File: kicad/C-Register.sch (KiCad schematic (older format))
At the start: 19 parts, among them U122 74LS245, U123 74LS173, U124 74LS173

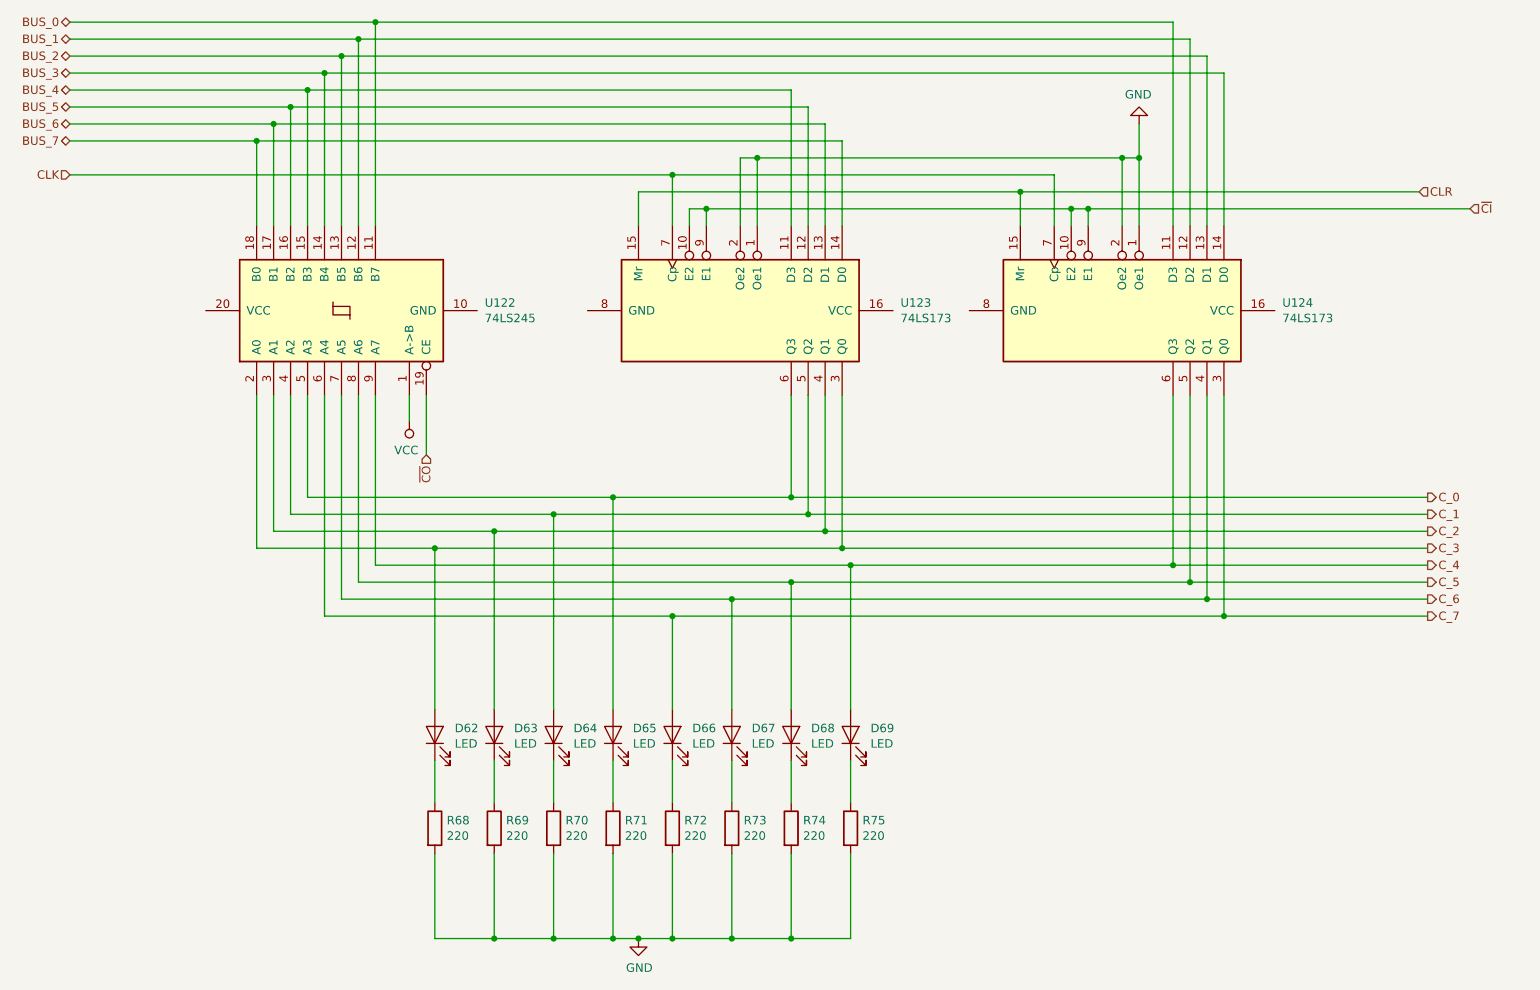
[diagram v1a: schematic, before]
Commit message: Reorganize part references
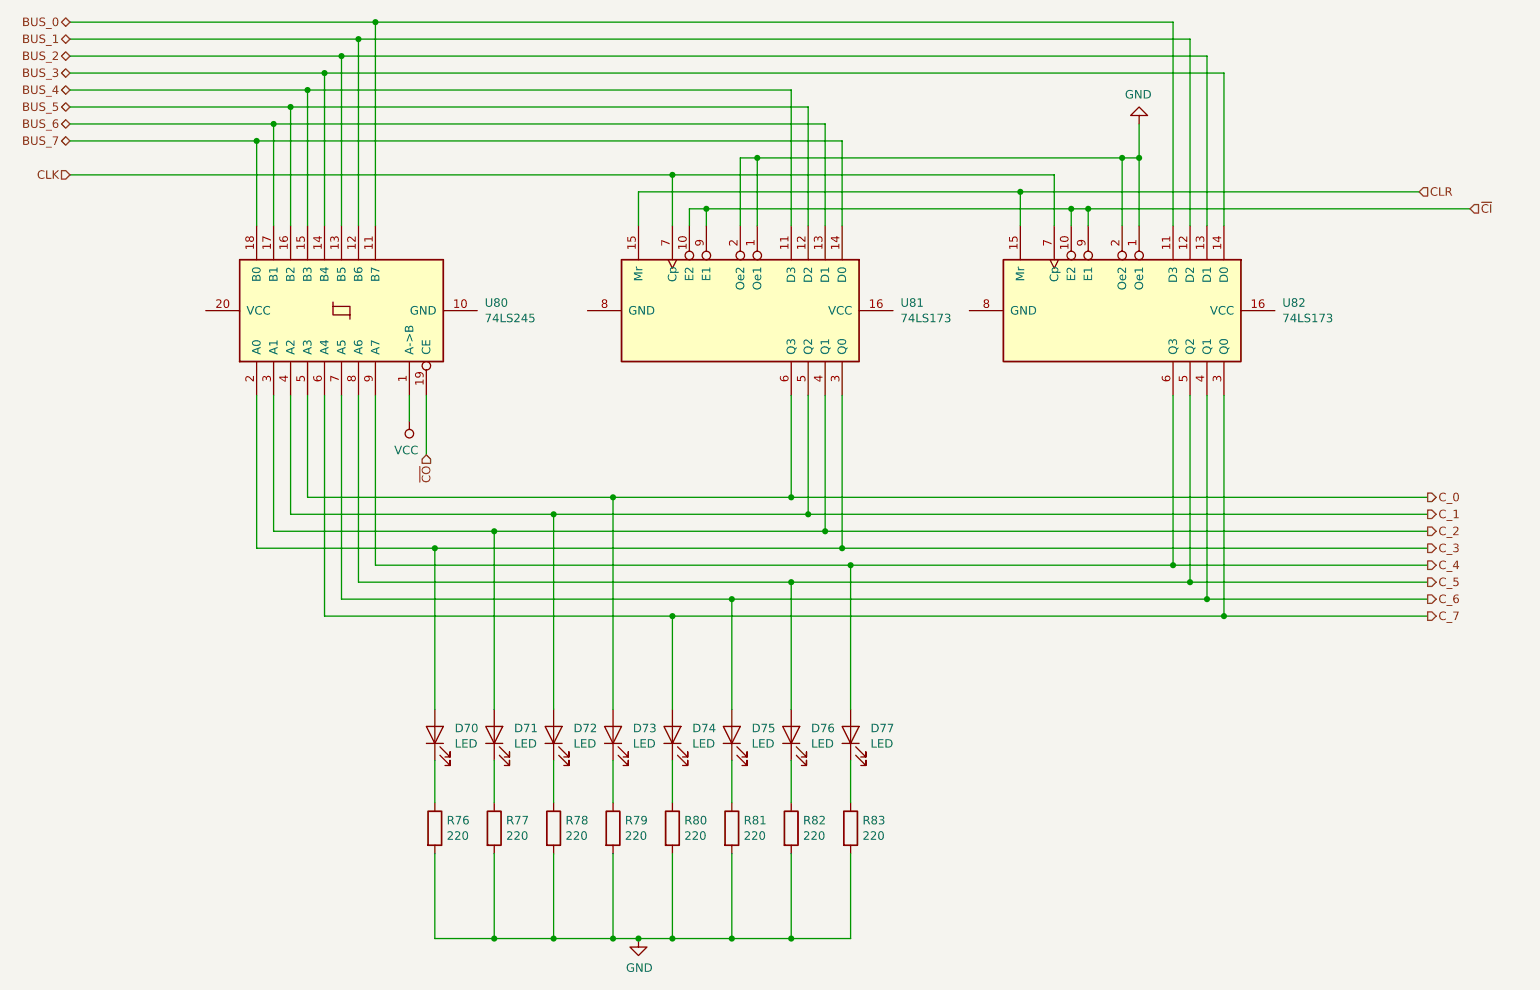
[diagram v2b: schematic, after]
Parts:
- renumbered D62 to D70, D63 to D71, D64 to D72, D65 to D73, D66 to D74, D67 to D75, D68 to D76, D69 to D77, R68 to R76, R69 to R77, R70 to R78, R71 to R79, R72 to R80, R73 to R81, R74 to R82, R75 to R83, U122 to U80, U123 to U81, U124 to U82
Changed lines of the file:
@@
 $Descr USLetter 11000 8500
 encoding utf-8
-Sheet 6 26
+Sheet 22 26
 Title "C Register"
 Date "2019-10-03"
@@
 AR Path="/5D9C722C/5D9DFD2F" Ref="U?"  Part="1"
 AR Path="/5D9DCC2F/5D9DFD2F" Ref="U?"  Part="1"
-AR Path="/5DA98D6D/5DA9A59D/5D9DFD2F" Ref="U122"  Part="1"
-F 0 "U122" V 3396 1956 50  0000 R CNN
+AR Path="/5DA98D6D/5DA9A59D/5D9DFD2F" Ref="U80"  Part="1"
+F 0 "U80" V 3396 1956 50  0000 R CNN
 F 1 "74LS245" V 3305 1956 50  0000 R CNN
 F 2 "" H 3350 2800 50  0001 C CNN
@@
 AR Path="/5D9C722C/5D9DFD5C" Ref="U?"  Part="1"
 AR Path="/5D9DCC2F/5D9DFD5C" Ref="U?"  Part="1"
-AR Path="/5DA98D6D/5DA9A59D/5D9DFD5C" Ref="U124"  Part="1"
-F 0 "U124" V 7904 3744 50  0000 L CNN
+AR Path="/5DA98D6D/5DA9A59D/5D9DFD5C" Ref="U82"  Part="1"
+F 0 "U82" V 7904 3744 50  0000 L CNN
 F 1 "74LS173" V 7995 3744 50  0000 L CNN
 F 2 "" H 7950 2800 50  0001 C CNN
@@
 AR Path="/5D9C722C/5D9DFD86" Ref="D?"  Part="1"
 AR Path="/5D9DCC2F/5D9DFD86" Ref="D?"  Part="1"
-AR Path="/5DA98D6D/5DA9A59D/5D9DFD86" Ref="D62"  Part="1"
-F 0 "D62" V 3939 5183 50  0000 R CNN
+AR Path="/5DA98D6D/5DA9A59D/5D9DFD86" Ref="D70"  Part="1"
+F 0 "D70" V 3939 5183 50  0000 R CNN
 F 1 "LED" V 3848 5183 50  0000 R CNN
 F 2 "" H 3900 5300 50  0001 C CNN
@@
 AR Path="/5D9C722C/5D9DFD8C" Ref="D?"  Part="1"
 AR Path="/5D9DCC2F/5D9DFD8C" Ref="D?"  Part="1"
-AR Path="/5DA98D6D/5DA9A59D/5D9DFD8C" Ref="D63"  Part="1"
-F 0 "D63" V 4289 5183 50  0000 R CNN
+AR Path="/5DA98D6D/5DA9A59D/5D9DFD8C" Ref="D71"  Part="1"
+F 0 "D71" V 4289 5183 50  0000 R CNN
 F 1 "LED" V 4198 5183 50  0000 R CNN
 F 2 "" H 4250 5300 50  0001 C CNN
@@
 AR Path="/5D9C722C/5D9DFD92" Ref="D?"  Part="1"
 AR Path="/5D9DCC2F/5D9DFD92" Ref="D?"  Part="1"
-AR Path="/5DA98D6D/5DA9A59D/5D9DFD92" Ref="D64"  Part="1"
-F 0 "D64" V 4639 5183 50  0000 R CNN
+AR Path="/5DA98D6D/5DA9A59D/5D9DFD92" Ref="D72"  Part="1"
+F 0 "D72" V 4639 5183 50  0000 R CNN
 F 1 "LED" V 4548 5183 50  0000 R CNN
 F 2 "" H 4600 5300 50  0001 C CNN
@@
 AR Path="/5D9C722C/5D9DFD98" Ref="D?"  Part="1"
 AR Path="/5D9DCC2F/5D9DFD98" Ref="D?"  Part="1"
-AR Path="/5DA98D6D/5DA9A59D/5D9DFD98" Ref="D65"  Part="1"
-F 0 "D65" V 4989 5183 50  0000 R CNN
+AR Path="/5DA98D6D/5DA9A59D/5D9DFD98" Ref="D73"  Part="1"
+F 0 "D73" V 4989 5183 50  0000 R CNN
 F 1 "LED" V 4898 5183 50  0000 R CNN
 F 2 "" H 4950 5300 50  0001 C CNN
@@
 AR Path="/5D9C722C/5D9DFD9E" Ref="D?"  Part="1"
 AR Path="/5D9DCC2F/5D9DFD9E" Ref="D?"  Part="1"
-AR Path="/5DA98D6D/5DA9A59D/5D9DFD9E" Ref="D66"  Part="1"
-F 0 "D66" V 5339 5183 50  0000 R CNN
+AR Path="/5DA98D6D/5DA9A59D/5D9DFD9E" Ref="D74"  Part="1"
+F 0 "D74" V 5339 5183 50  0000 R CNN
 F 1 "LED" V 5248 5183 50  0000 R CNN
 F 2 "" H 5300 5300 50  0001 C CNN
@@
 AR Path="/5D9C722C/5D9DFDA4" Ref="D?"  Part="1"
 AR Path="/5D9DCC2F/5D9DFDA4" Ref="D?"  Part="1"
-AR Path="/5DA98D6D/5DA9A59D/5D9DFDA4" Ref="D67"  Part="1"
-F 0 "D67" V 5689 5183 50  0000 R CNN
+AR Path="/5DA98D6D/5DA9A59D/5D9DFDA4" Ref="D75"  Part="1"
+F 0 "D75" V 5689 5183 50  0000 R CNN
 F 1 "LED" V 5598 5183 50  0000 R CNN
 F 2 "" H 5650 5300 50  0001 C CNN
@@
 AR Path="/5D9C722C/5D9DFDAA" Ref="D?"  Part="1"
 AR Path="/5D9DCC2F/5D9DFDAA" Ref="D?"  Part="1"
-AR Path="/5DA98D6D/5DA9A59D/5D9DFDAA" Ref="D68"  Part="1"
-F 0 "D68" V 6039 5183 50  0000 R CNN
+AR Path="/5DA98D6D/5DA9A59D/5D9DFDAA" Ref="D76"  Part="1"
+F 0 "D76" V 6039 5183 50  0000 R CNN
 F 1 "LED" V 5948 5183 50  0000 R CNN
 F 2 "" H 6000 5300 50  0001 C CNN
@@
 AR Path="/5D9C722C/5D9DFDB0" Ref="D?"  Part="1"
 AR Path="/5D9DCC2F/5D9DFDB0" Ref="D?"  Part="1"
-AR Path="/5DA98D6D/5DA9A59D/5D9DFDB0" Ref="D69"  Part="1"
-F 0 "D69" V 6389 5183 50  0000 R CNN
+AR Path="/5DA98D6D/5DA9A59D/5D9DFDB0" Ref="D77"  Part="1"
+F 0 "D77" V 6389 5183 50  0000 R CNN
 F 1 "LED" V 6298 5183 50  0000 R CNN
 F 2 "" H 6350 5300 50  0001 C CNN
@@
 AR Path="/5D9C722C/5D9DFDCC" Ref="R?"  Part="1"
 AR Path="/5D9DCC2F/5D9DFDCC" Ref="R?"  Part="1"
-AR Path="/5DA98D6D/5DA9A59D/5D9DFDCC" Ref="R68"  Part="1"
-F 0 "R68" H 3970 5896 50  0000 L CNN
+AR Path="/5DA98D6D/5DA9A59D/5D9DFDCC" Ref="R76"  Part="1"
+F 0 "R76" H 3970 5896 50  0000 L CNN
 F 1 "220" H 3970 5805 50  0000 L CNN
 F 2 "" V 3830 5850 50  0001 C CNN
@@
 AR Path="/5D9C722C/5D9DFDD2" Ref="R?"  Part="1"
 AR Path="/5D9DCC2F/5D9DFDD2" Ref="R?"  Part="1"
-AR Path="/5DA98D6D/5DA9A59D/5D9DFDD2" Ref="R69"  Part="1"
-F 0 "R69" H 4320 5896 50  0000 L CNN
+AR Path="/5DA98D6D/5DA9A59D/5D9DFDD2" Ref="R77"  Part="1"
+F 0 "R77" H 4320 5896 50  0000 L CNN
 F 1 "220" H 4320 5805 50  0000 L CNN
 F 2 "" V 4180 5850 50  0001 C CNN
@@
 AR Path="/5D9C722C/5D9DFDD8" Ref="R?"  Part="1"
 AR Path="/5D9DCC2F/5D9DFDD8" Ref="R?"  Part="1"
-AR Path="/5DA98D6D/5DA9A59D/5D9DFDD8" Ref="R70"  Part="1"
-F 0 "R70" H 4670 5896 50  0000 L CNN
+AR Path="/5DA98D6D/5DA9A59D/5D9DFDD8" Ref="R78"  Part="1"
+F 0 "R78" H 4670 5896 50  0000 L CNN
 F 1 "220" H 4670 5805 50  0000 L CNN
 F 2 "" V 4530 5850 50  0001 C CNN
@@
 AR Path="/5D9C722C/5D9DFDDE" Ref="R?"  Part="1"
 AR Path="/5D9DCC2F/5D9DFDDE" Ref="R?"  Part="1"
-AR Path="/5DA98D6D/5DA9A59D/5D9DFDDE" Ref="R71"  Part="1"
-F 0 "R71" H 5020 5896 50  0000 L CNN
+AR Path="/5DA98D6D/5DA9A59D/5D9DFDDE" Ref="R79"  Part="1"
+F 0 "R79" H 5020 5896 50  0000 L CNN
 F 1 "220" H 5020 5805 50  0000 L CNN
 F 2 "" V 4880 5850 50  0001 C CNN
@@
 AR Path="/5D9C722C/5D9DFDE4" Ref="R?"  Part="1"
 AR Path="/5D9DCC2F/5D9DFDE4" Ref="R?"  Part="1"
-AR Path="/5DA98D6D/5DA9A59D/5D9DFDE4" Ref="R72"  Part="1"
-F 0 "R72" H 5370 5896 50  0000 L CNN
+AR Path="/5DA98D6D/5DA9A59D/5D9DFDE4" Ref="R80"  Part="1"
+F 0 "R80" H 5370 5896 50  0000 L CNN
 F 1 "220" H 5370 5805 50  0000 L CNN
 F 2 "" V 5230 5850 50  0001 C CNN
@@
 AR Path="/5D9C722C/5D9DFDEA" Ref="R?"  Part="1"
 AR Path="/5D9DCC2F/5D9DFDEA" Ref="R?"  Part="1"
-AR Path="/5DA98D6D/5DA9A59D/5D9DFDEA" Ref="R73"  Part="1"
-F 0 "R73" H 5720 5896 50  0000 L CNN
+AR Path="/5DA98D6D/5DA9A59D/5D9DFDEA" Ref="R81"  Part="1"
+F 0 "R81" H 5720 5896 50  0000 L CNN
 F 1 "220" H 5720 5805 50  0000 L CNN
 F 2 "" V 5580 5850 50  0001 C CNN
@@
 AR Path="/5D9C722C/5D9DFDF0" Ref="R?"  Part="1"
 AR Path="/5D9DCC2F/5D9DFDF0" Ref="R?"  Part="1"
-AR Path="/5DA98D6D/5DA9A59D/5D9DFDF0" Ref="R74"  Part="1"
-F 0 "R74" H 6070 5896 50  0000 L CNN
+AR Path="/5DA98D6D/5DA9A59D/5D9DFDF0" Ref="R82"  Part="1"
+F 0 "R82" H 6070 5896 50  0000 L CNN
 F 1 "220" H 6070 5805 50  0000 L CNN
 F 2 "" V 5930 5850 50  0001 C CNN
@@
 AR Path="/5D9C722C/5D9DFDF6" Ref="R?"  Part="1"
 AR Path="/5D9DCC2F/5D9DFDF6" Ref="R?"  Part="1"
-AR Path="/5DA98D6D/5DA9A59D/5D9DFDF6" Ref="R75"  Part="1"
-F 0 "R75" H 6420 5896 50  0000 L CNN
+AR Path="/5DA98D6D/5DA9A59D/5D9DFDF6" Ref="R83"  Part="1"
+F 0 "R83" H 6420 5896 50  0000 L CNN
 F 1 "220" H 6420 5805 50  0000 L CNN
 F 2 "" V 6280 5850 50  0001 C CNN
@@
 AR Path="/5D9C722C/5D9DFE47" Ref="U?"  Part="1"
 AR Path="/5D9DCC2F/5D9DFE47" Ref="U?"  Part="1"
-AR Path="/5DA98D6D/5DA9A59D/5D9DFE47" Ref="U123"  Part="1"
-F 0 "U123" V 5654 3744 50  0000 L CNN
+AR Path="/5DA98D6D/5DA9A59D/5D9DFE47" Ref="U81"  Part="1"
+F 0 "U81" V 5654 3744 50  0000 L CNN
 F 1 "74LS173" V 5745 3744 50  0000 L CNN
 F 2 "" H 5700 2800 50  0001 C CNN
